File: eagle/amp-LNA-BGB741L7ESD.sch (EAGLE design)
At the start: 19 parts, among them J1 142-0701-851, J2 142-0701-851, Q1 PMOS, U1 BGB7XXL7ESD

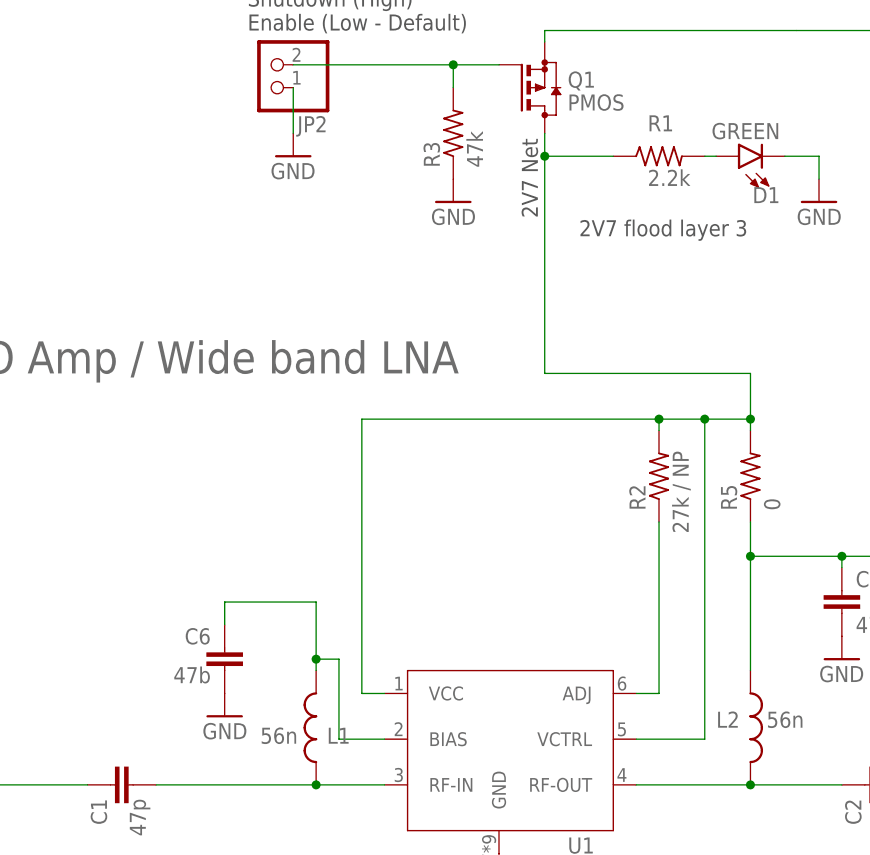
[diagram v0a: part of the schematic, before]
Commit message: BGB741 update values
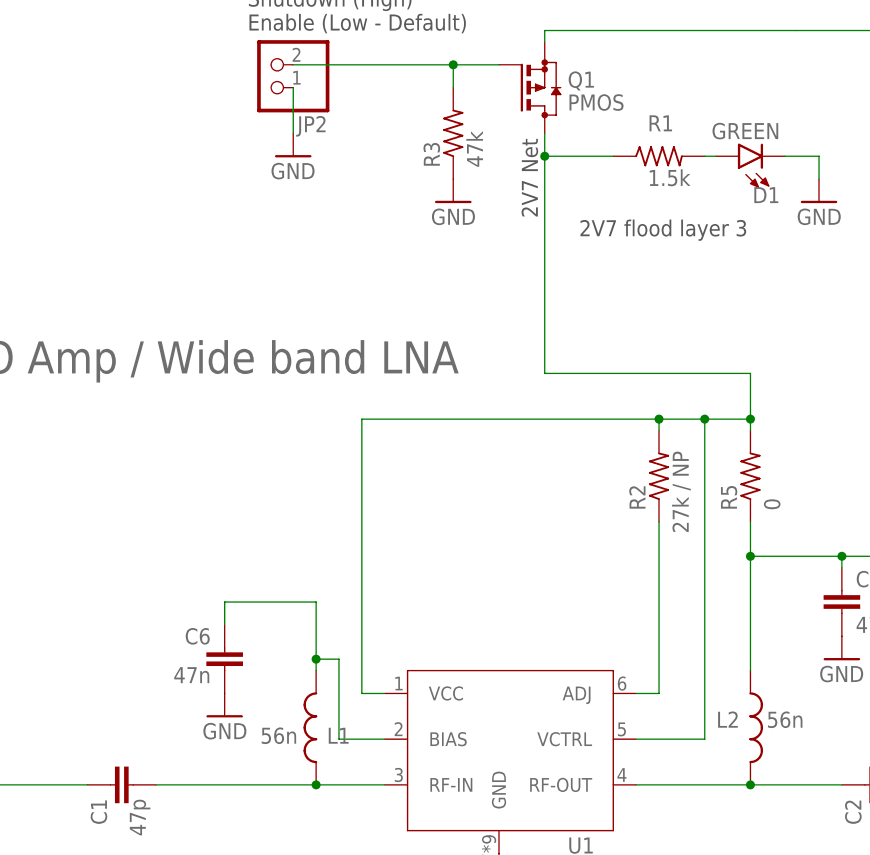
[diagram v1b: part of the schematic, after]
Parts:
- C6: value 47b -> 47n
- R1: value 2.2k -> 1.5k
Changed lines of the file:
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@@
 </part>
 <part name="GND80" library="supply1" deviceset="GND" device=""/>
-<part name="R1" library="oresat-rcl" deviceset="R-US_" device="0603-B-NOSILK" value="2.2k"/>
+<part name="R1" library="oresat-rcl" deviceset="R-US_" device="0603-B-NOSILK" value="1.5k"/>
 <part name="J1" library="J-Cinch-142-0701-851-SMA-end-launch" deviceset="142-0701-851" device=""/>
 <part name="J2" library="J-Cinch-142-0701-851-SMA-end-launch" deviceset="142-0701-851" device=""/>
@@
 <part name="GND7" library="supply1" library_urn="urn:adsk.eagle:library:371" deviceset="GND" device=""/>
 <part name="GND8" library="supply1" library_urn="urn:adsk.eagle:library:371" deviceset="GND" device=""/>
-<part name="C6" library="oresat-rcl" deviceset="C-EU" device="0603-B-NOSILK" value="47b"/>
+<part name="C6" library="oresat-rcl" deviceset="C-EU" device="0603-B-NOSILK" value="47n"/>
 <part name="Q1" library="transistor-small-signal" library_urn="urn:adsk.eagle:library:401" deviceset="BSS84" device="" package3d_urn="urn:adsk.eagle:package:28738/2" value="PMOS"/>
 <part name="JP2" library="pinhead" library_urn="urn:adsk.eagle:library:325" deviceset="PINHD-1X2" device="" package3d_urn="urn:adsk.eagle:package:22435/2"/>
